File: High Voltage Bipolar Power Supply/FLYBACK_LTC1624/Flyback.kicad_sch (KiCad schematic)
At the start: 43 parts, among them J2 1715721, Q1 PZT2222A, Q2 IRL540NS, T1 VERSA-PAC, U1 LTC1624CS8, U4 TSR_1-2450, U5 TBA1-2411E

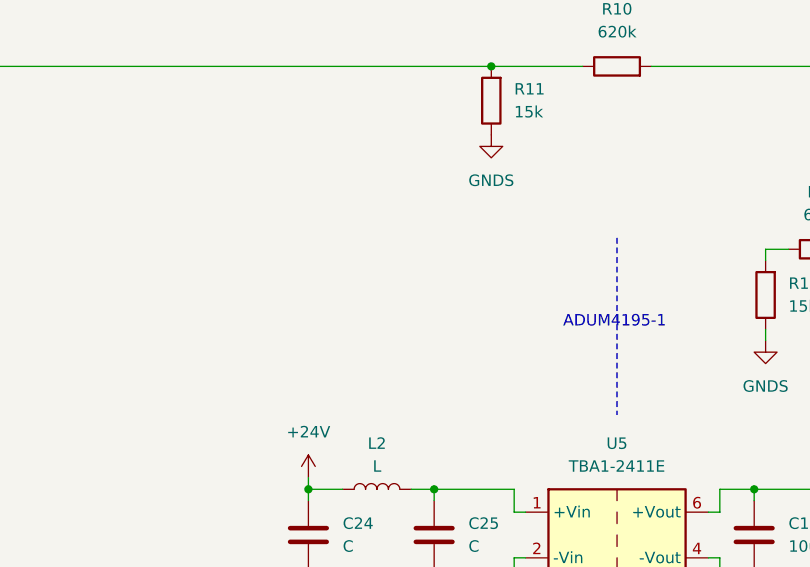
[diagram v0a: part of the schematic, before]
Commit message: FLYBACK_LTC1624 : Schematic desing
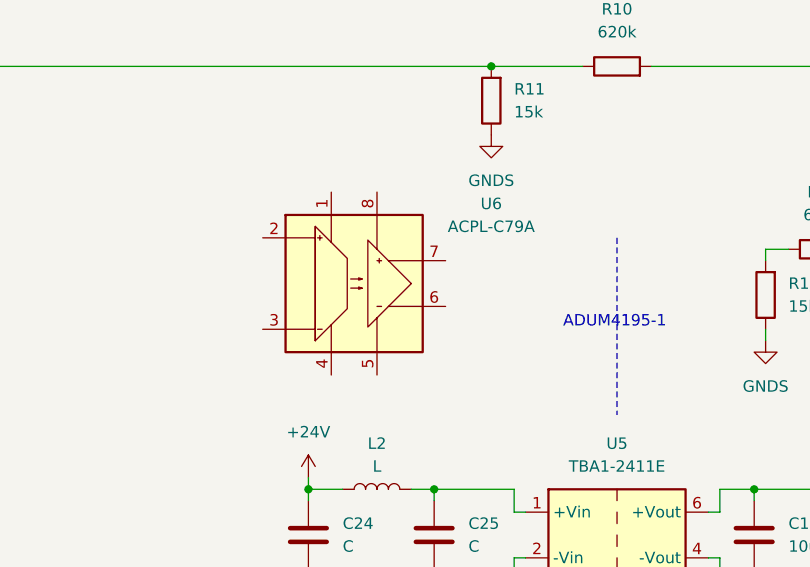
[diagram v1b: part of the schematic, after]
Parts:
- added U6: ACPL-C79A, Package_SO:SSO-8_6.8x5.9mm_P1.27mm_Clearance8mm, symbol Isolator_Analog:ACPL-C79A
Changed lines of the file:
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@@
+	)
+	(symbol
+		(lib_id "Isolator_Analog:ACPL-C79A")
+		(at 130.81 123.19 0)
+		(unit 1)
+		(exclude_from_sim no)
+		(in_bom yes)
+		(on_board yes)
+		(dnp no)
+		(fields_autoplaced yes)
+		(property "Reference" "U6"
+			(at 146.05 114.3314 0)
+			(effects
+				(font
+					(size 1.27 1.27)
+				)
+			)
+		)
+		(property "Value" "ACPL-C79A"
+			(at 146.05 116.8714 0)
+			(effects
+				(font
+					(size 1.27 1.27)
+				)
+			)
+		)
+		(property "Footprint" "Package_SO:SSO-8_6.8x5.9mm_P1.27mm_Clearance8mm"
+			(at 134.62 132.08 0)
+			(effects
+				(font
+					(size 1.27 1.27)
+					(italic yes)
+				)
+				(justify left)
+				(hide yes)
+			)
+		)
+		(property "Datasheet" "http://docs.avagotech.com/docs/AV02-2460EN"
+			(at 131.953 123.063 0)
+			(effects
+				(font
+					(size 1.27 1.27)
+				)
+				(justify left)
+				(hide yes)
+			)
+		)
+		(property "Description" "Precision Isolation Amplifer, ±1% Gain Tolerance, Bandwidth 200kHz, SSO-8"
+			(at 130.81 123.19 0)
+			(effects
+				(font
+					(size 1.27 1.27)
+				)
+				(hide yes)
+			)
+		)
+		(pin "4"
+		)
+		(pin "5"
+		)
+		(pin "7"
+		)
+		(pin "6"
+		)
+		(pin "2"
+		)
+		(pin "3"
+		)
+		(pin "8"
+		)
+		(pin "1"
+		)
+		(instances
+			(project ""
+				(path "/b6dc4b50-1aef-431e-aae5-8ba2077040d1/0d0ff0c8-e715-47fe-aebe-0044b1d841d2"
+					(reference "U6")
+					(unit 1)
+				)
+			)
+		)
 	)
 	(symbol

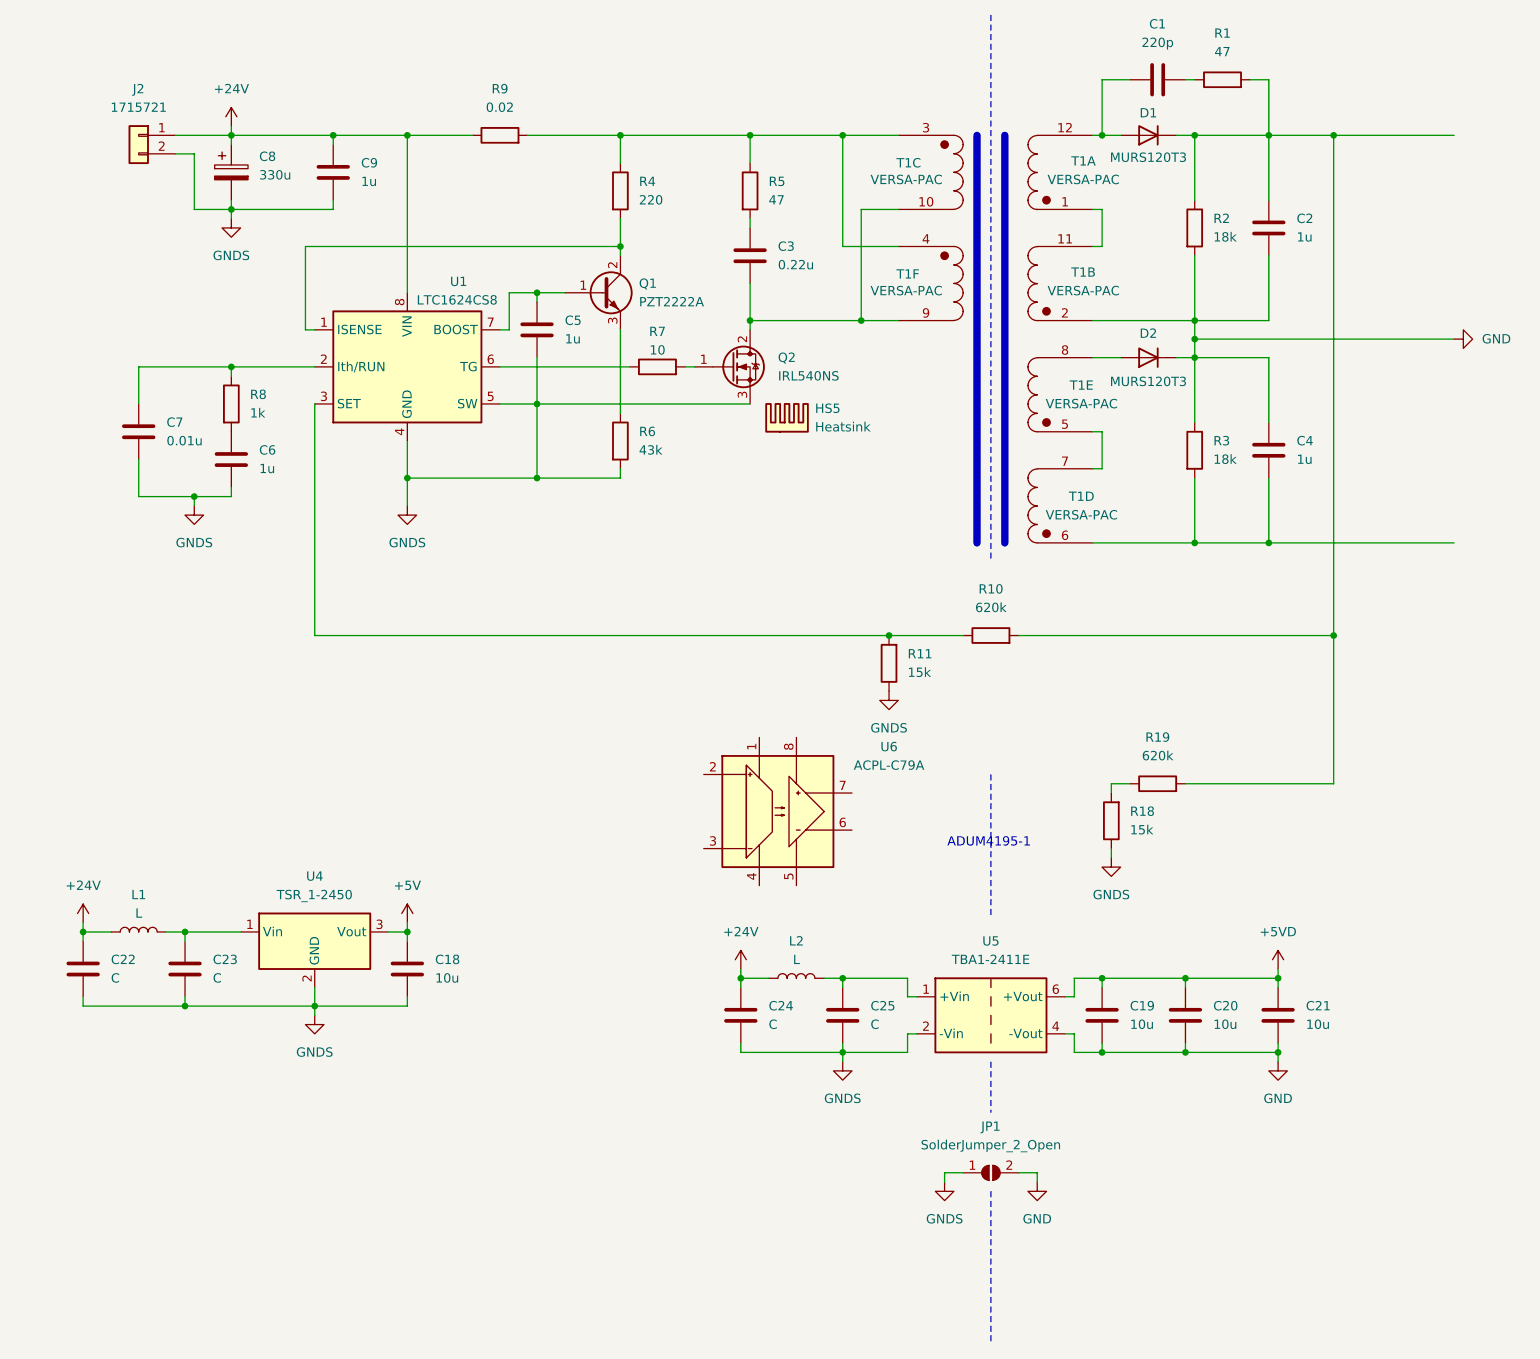
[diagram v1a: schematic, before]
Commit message: FLYBACK_LTC1624 : Schematic desing
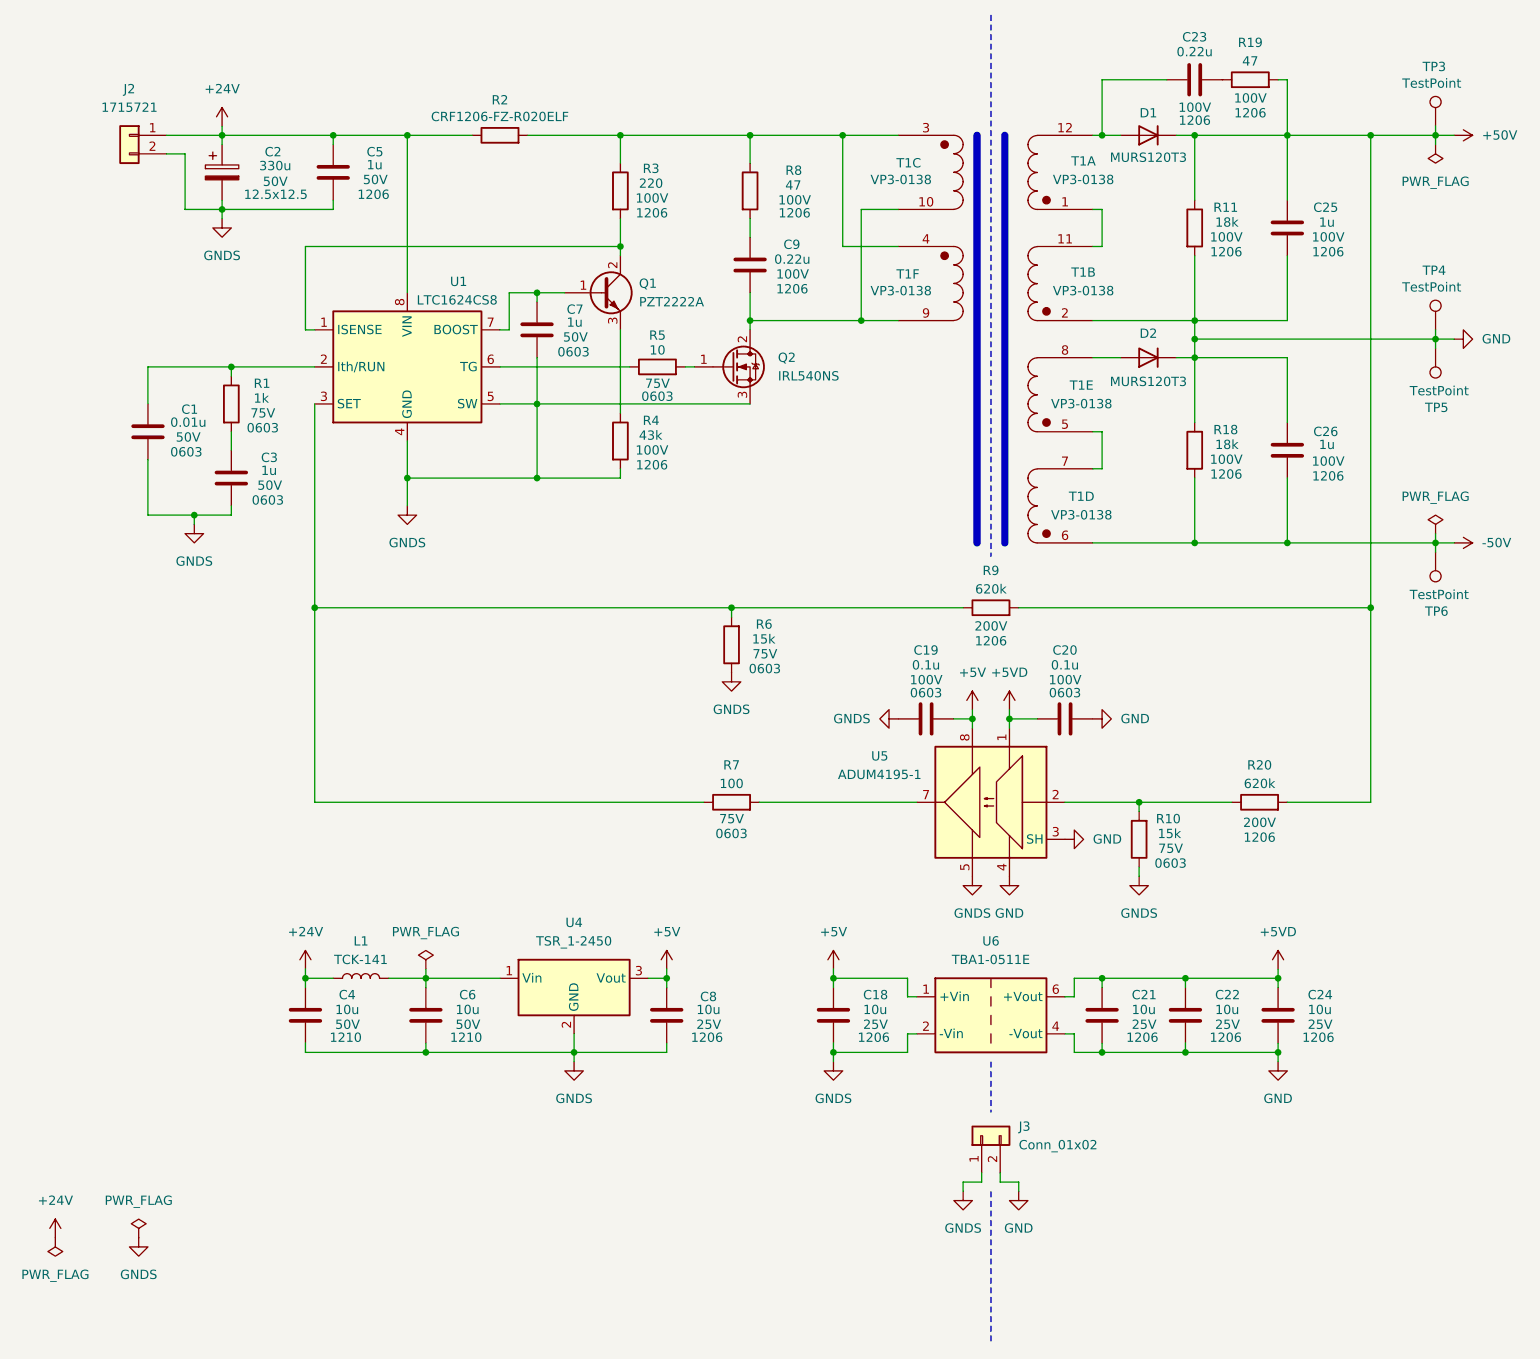
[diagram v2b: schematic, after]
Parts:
- removed C2, C5: 1u, symbol Device:C
- removed HS5: Heatsink, symbol Mechanical:Heatsink
- removed JP1: SolderJumper_2_Open, symbol Jumper:SolderJumper_2_Open
- removed L2: L, symbol Device:L
- removed R2: 18k, symbol Device:R
- removed R8: 1k, symbol Device:R
- removed U5: TBA1-2411E, Converter_DCDC:Converter_DCDC_TRACO_TBA1-xxxxE_Single_THT, symbol Converter_DCDC:TBA1-2411E
- removed U6: ACPL-C79A, Package_SO:SSO-8_6.8x5.9mm_P1.27mm_Clearance8mm, symbol Isolator_Analog:ACPL-C79A
- added C4: 10u, Capacitor_SMD:C_1210_3225Metric_Pad1.33x2.70mm_HandSolder, symbol Device:C
- added C8: 10u, Capacitor_SMD:C_1206_3216Metric_Pad1.33x1.80mm_HandSolder, symbol Device:C
- added C9: 0.22u, Capacitor_SMD:C_1206_3216Metric_Pad1.33x1.80mm_HandSolder, symbol Device:C
- added J3: Conn_01x02, Connector_PinHeader_2.54mm:PinHeader_1x02_P2.54mm_Vertical, symbol Connector_Generic:Conn_01x02
- added R19: 47, Resistor_SMD:R_1206_3216Metric_Pad1.30x1.75mm_HandSolder, symbol Device:R
- added R5: 10, Resistor_SMD:R_0603_1608Metric_Pad0.98x0.95mm_HandSolder, symbol Device:R
- added R6: 15k, Resistor_SMD:R_0603_1608Metric_Pad0.98x0.95mm_HandSolder, symbol Device:R
- added TP3, TP4, TP5, TP6: TestPoint, TestPoint:TestPoint_THTPad_D3.0mm_Drill1.5mm, symbol Connector:TestPoint
- added U5: ADUM4195-1, Package_SO:SSO-8_6.8x5.9mm_P1.27mm_Clearance8mm, symbol FLYBACK_LTC1624:ADUM4195-1
- added U6: TBA1-0511E, Converter_DCDC:Converter_DCDC_TRACO_TBA1-xxxxE_Single_THT, symbol Converter_DCDC:TBA1-0511E
- C1: value 220p -> 0.01u; footprint (none) -> Capacitor_SMD:C_0603_1608Metric_Pad1.08x0.95mm_HandSolder; Package (none) -> 0603; Voltage (none) -> 50V
- C18, C21: footprint (none) -> Capacitor_SMD:C_1206_3216Metric_Pad1.33x1.80mm_HandSolder; Package (none) -> 1206; Voltage (none) -> 25V
- C19, C20: value 10u -> 0.1u; footprint (none) -> Capacitor_SMD:C_0603_1608Metric_Pad1.08x0.95mm_HandSolder; Package (none) -> 0603; Voltage (none) -> 100V
- C2: renamed from C8; footprint (none) -> Capacitor_SMD:CP_Elec_10x10; Package (none) -> 12.5x12.5; Voltage (none) -> 50V
- C22, C24: value C -> 10u; footprint (none) -> Capacitor_SMD:C_1206_3216Metric_Pad1.33x1.80mm_HandSolder; Package (none) -> 1206; Voltage (none) -> 25V
- C23: value C -> 0.22u; footprint (none) -> Capacitor_SMD:C_1206_3216Metric_Pad1.33x1.80mm_HandSolder; Package (none) -> 1206; Voltage (none) -> 100V
- C25: value C -> 1u; footprint (none) -> Capacitor_SMD:C_1206_3216Metric_Pad1.33x1.80mm_HandSolder; Package (none) -> 1206; Voltage (none) -> 100V
- C26: renamed from C4; footprint (none) -> Capacitor_SMD:C_1206_3216Metric_Pad1.33x1.80mm_HandSolder; Package (none) -> 1206; Voltage (none) -> 100V
- C3: value 0.22u -> 1u; footprint (none) -> Capacitor_SMD:C_0603_1608Metric_Pad1.08x0.95mm_HandSolder; Package (none) -> 0603; Voltage (none) -> 50V
- C5: renamed from C9; footprint (none) -> Capacitor_SMD:C_1206_3216Metric_Pad1.33x1.80mm_HandSolder; Package (none) -> 1206; Voltage (none) -> 50V
- C6: value 1u -> 10u; footprint (none) -> Capacitor_SMD:C_1210_3225Metric_Pad1.33x2.70mm_HandSolder; Package (none) -> 1210; Voltage (none) -> 50V
- C7: value 0.01u -> 1u; footprint (none) -> Capacitor_SMD:C_0603_1608Metric_Pad1.08x0.95mm_HandSolder; Package (none) -> 0603; Voltage (none) -> 50V
- D1, D2: footprint (none) -> Diode_SMD:D_SMB
- L1: value L -> TCK-141; footprint (none) -> FLYBACK_LTC1624:TCK-141
- Q2: footprint (none) -> Package_TO_SOT_SMD:TO-263-2
- R1: value 47 -> 1k; footprint (none) -> Resistor_SMD:R_0603_1608Metric_Pad0.98x0.95mm_HandSolder; Package (none) -> 0603; Voltage (none) -> 75V
- R10: renamed from R18; footprint (none) -> Resistor_SMD:R_0603_1608Metric_Pad0.98x0.95mm_HandSolder; Package (none) -> 0603; Voltage (none) -> 75V
- R11: value 15k -> 18k; footprint (none) -> Resistor_SMD:R_1206_3216Metric_Pad1.30x1.75mm_HandSolder; Package (none) -> 1206; Voltage (none) -> 100V
- R18: renamed from R3; footprint (none) -> Resistor_SMD:R_1206_3216Metric_Pad1.30x1.75mm_HandSolder; Package (none) -> 1206; Voltage (none) -> 100V
- R2: renamed from R9; value 0.02 -> CRF1206-FZ-R020ELF; footprint (none) -> Resistor_SMD:R_1206_3216Metric_Pad1.30x1.75mm_HandSolder
- R20: renamed from R19; footprint (none) -> Resistor_SMD:R_1206_3216Metric_Pad1.30x1.75mm_HandSolder; Package (none) -> 1206; Voltage (none) -> 200V
- R3: renamed from R4; footprint (none) -> Resistor_SMD:R_1206_3216Metric_Pad1.30x1.75mm_HandSolder; Package (none) -> 1206; Voltage (none) -> 100V
- R4: renamed from R6; footprint (none) -> Resistor_SMD:R_1206_3216Metric_Pad1.30x1.75mm_HandSolder; Package (none) -> 1206; Voltage (none) -> 100V
- R7: value 10 -> 100; footprint (none) -> Resistor_SMD:R_0603_1608Metric_Pad0.98x0.95mm_HandSolder; Package (none) -> 0603; Voltage (none) -> 75V
- R8: renamed from R5; footprint (none) -> Resistor_SMD:R_1206_3216Metric_Pad1.30x1.75mm_HandSolder; Package (none) -> 1206; Voltage (none) -> 100V
- R9: renamed from R10; footprint (none) -> Resistor_SMD:R_1206_3216Metric_Pad1.30x1.75mm_HandSolder; Package (none) -> 1206; Voltage (none) -> 200V
- T1: value VERSA-PAC -> VP3-0138; footprint (none) -> FLYBACK_LTC1624:VP3
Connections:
- net +24V: now also C4.1; no longer C22.1, C24.1
- net +5V: now also C19.2, C8.1, U5.8, U6.1 (+Vin)
- net +5VD: now also C22.1, C24.1, U5.1, U6.6 (+Vout); no longer C19.1
- net GND: now also C22.2, C24.2, C25.2, R11.2, J3.2 (Pin_2), TP4.1, TP5.1, U5.3 (SH), U5.4, U6.4 (-Vout); no longer C19.2
- net GNDS: now also C1.2, C19.1, C3.2, C4.2, C8.2, J3.1 (Pin_1), R6.1, U5.5, U6.2 (-Vin); no longer C22.2, C23.2, C24.2, C25.2, R11.1
- net at R10.2, R20.1: now also U5.2
- net +50V: now reaches C25.1
- net +50V: now also D1.1 (K), R11.1, R20.2, R9.2, R19.2, TP3.1
- net at R8.2: now also C9.1; no longer C3.1
- net at Q2.2 (D), T1.10, T1.9: now also C9.2; no longer C3.2
- net at R9.1, U1.3 (SET): now also R7.1, R6.2; no longer R11.2
- net at L1.2, U4.1 (Vin): now also C6.1; no longer C23.1
- net -50V: now reaches C26.2, R18.2, T1.6
- net -50V: now also TP6.1
- net at Q2.1 (G): now also R5.2; no longer R7.2
- net at Q1.1 (B), U1.7 (BOOST): now also C7.1
- net at U1.2 (Ith/RUN): now also C1.1, R1.1; no longer C7.1
- net at U1.6 (TG): now also R5.1; no longer R7.1
- net at D1.2 (A), T1.12: now also C23.1; no longer C1.1
- new net: C23.2, R19.1
- new net: C3.1, R1.2
- new net: R7.2, U5.7
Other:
- note removed: "ADUM4195-1"
- moved on the sheet: C2, C26, J2, L1, R10, R20, R9, U4

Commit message: FLYBACK_LTC1624: PCB layout
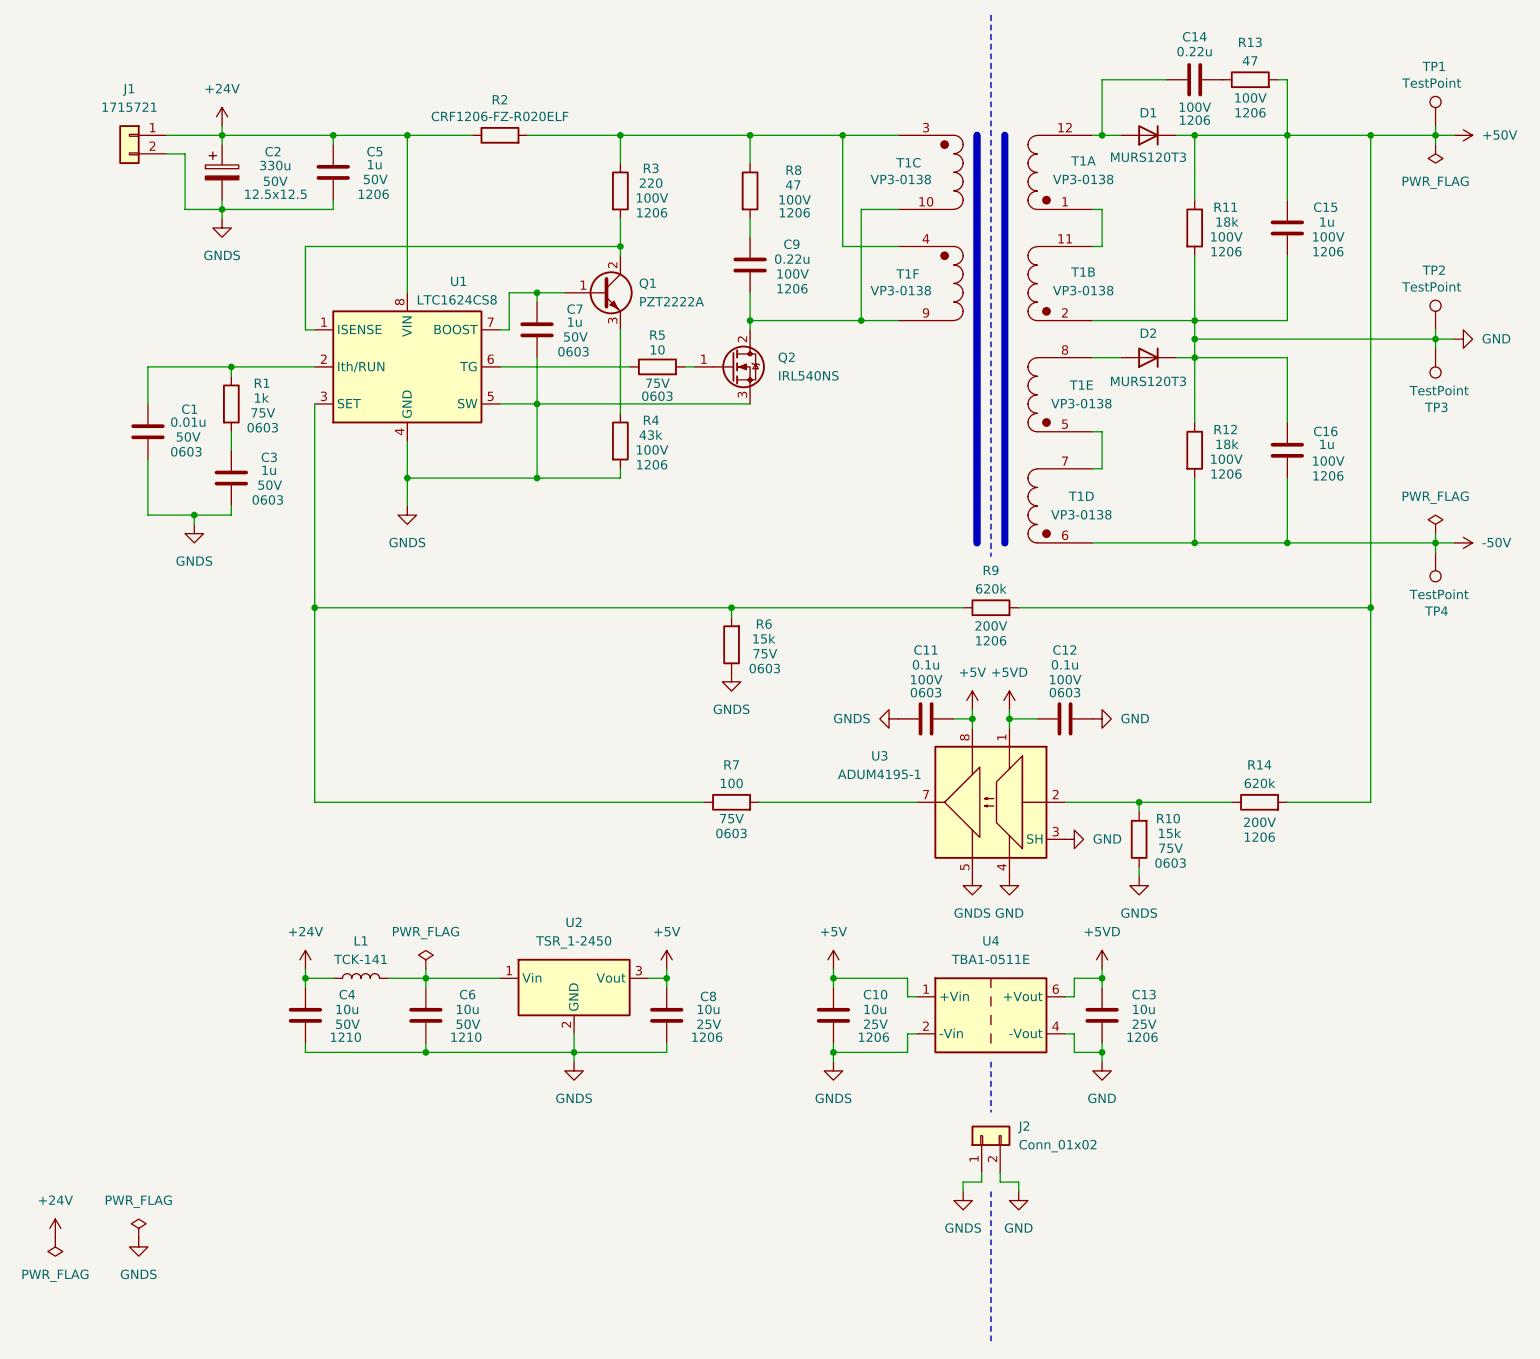
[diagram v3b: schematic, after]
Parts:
- removed C22, C24: 10u, Capacitor_SMD:C_1206_3216Metric_Pad1.33x1.80mm_HandSolder, symbol Device:C
- renumbered C18 to C10, C19 to C11, C20 to C12, C21 to C13, C23 to C14, C25 to C15, C26 to C16, J2 to J1, J3 to J2, R18 to R12, R19 to R13, R20 to R14, TP3 to TP1, TP4 to TP2, TP5 to TP3, TP6 to TP4, U4 to U2, U5 to U3, U6 to U4
